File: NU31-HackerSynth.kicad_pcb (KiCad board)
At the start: 2 copper layers, 180 x 110 mm, 135 parts, among them J1 Conn_02x07_Counter_Clockwise, J2 AudioJack3, J3 Barrel_Jack, J4 AudioJack2_SwitchT, J5 AudioJack2_SwitchT, J6 AudioJack2_SwitchT, J7 Eurorack Power, Q1 NPN, Q2 NPN, Q3 NPN, Q4 NPN, SW1 SW_DPDT, SW2 SW_SPDT, U1 LM358, U2 LM358, U3 LM358, U4 CD4017, U5 LM358, U6 LM358, U7 LM358

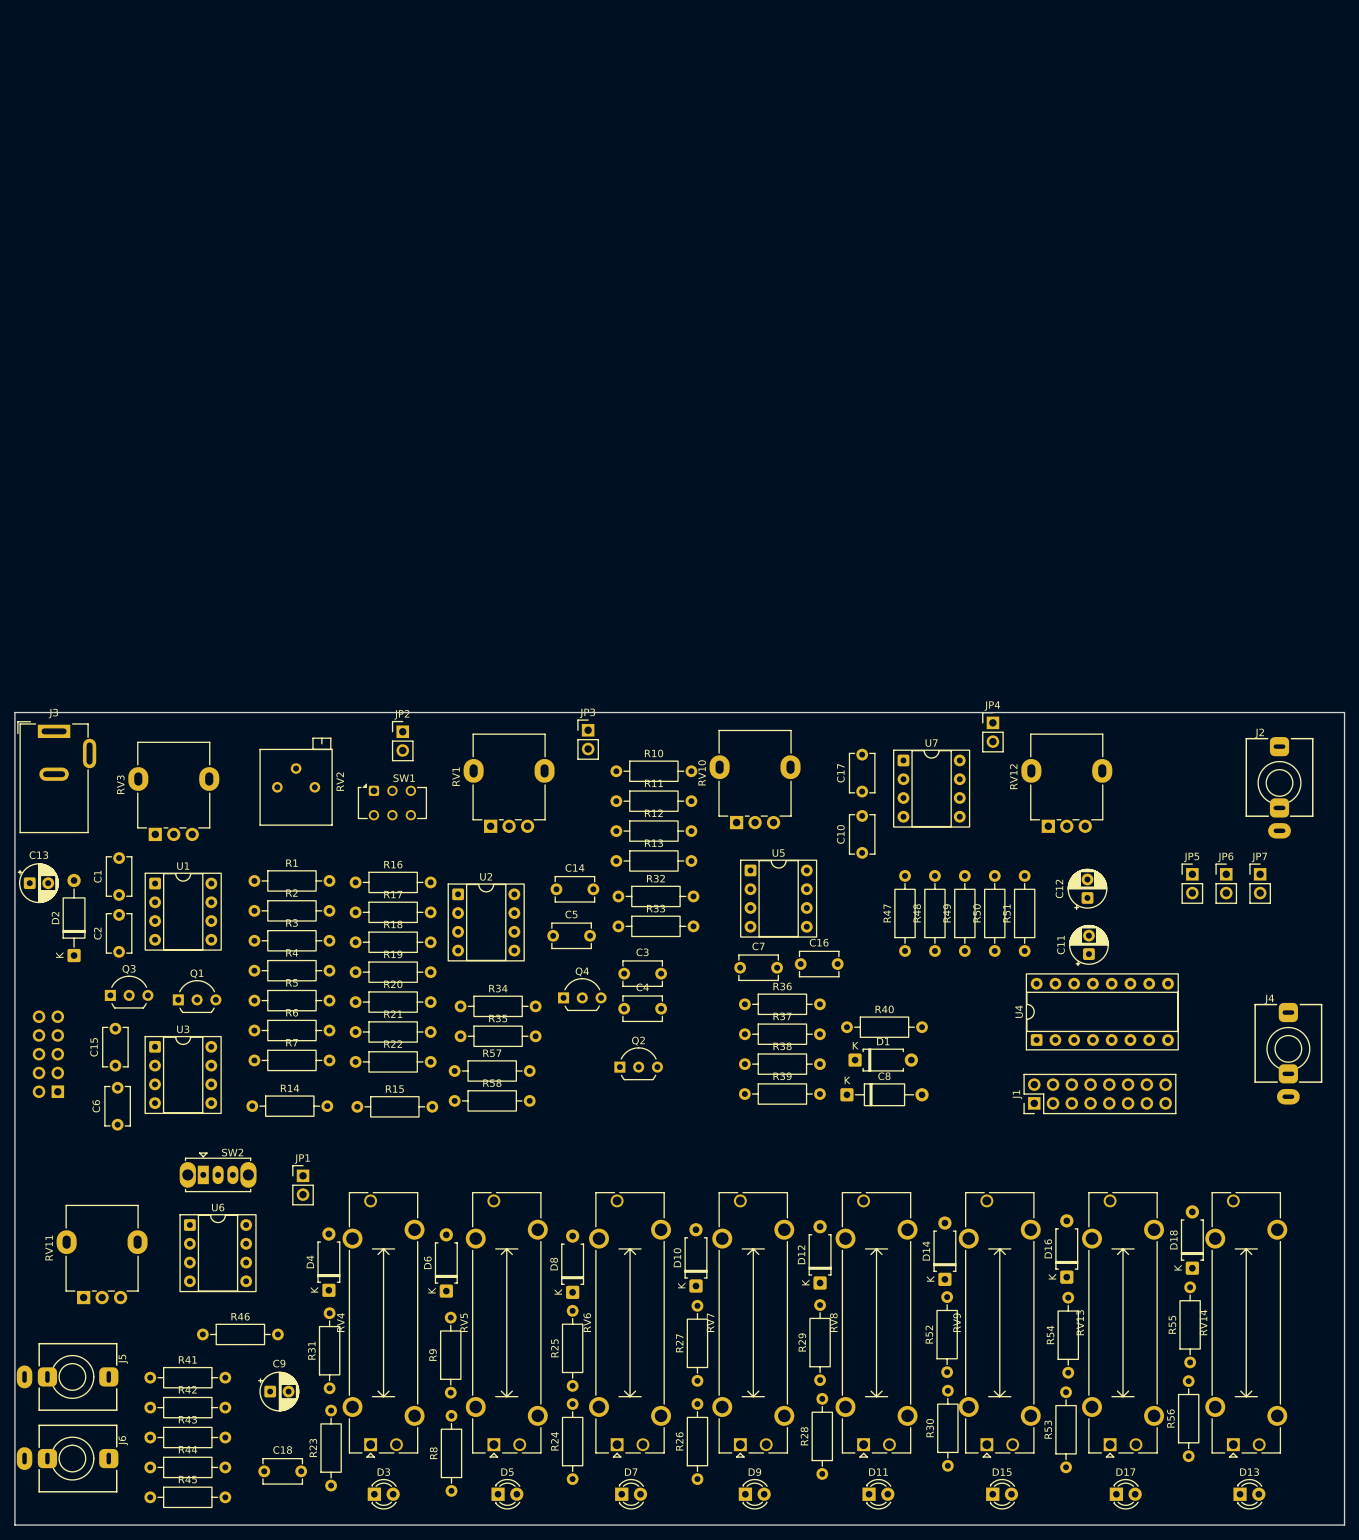
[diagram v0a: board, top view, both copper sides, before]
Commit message: Added negative voltage protection for sequencer clock input, added footprints for faders and rotaryswitch
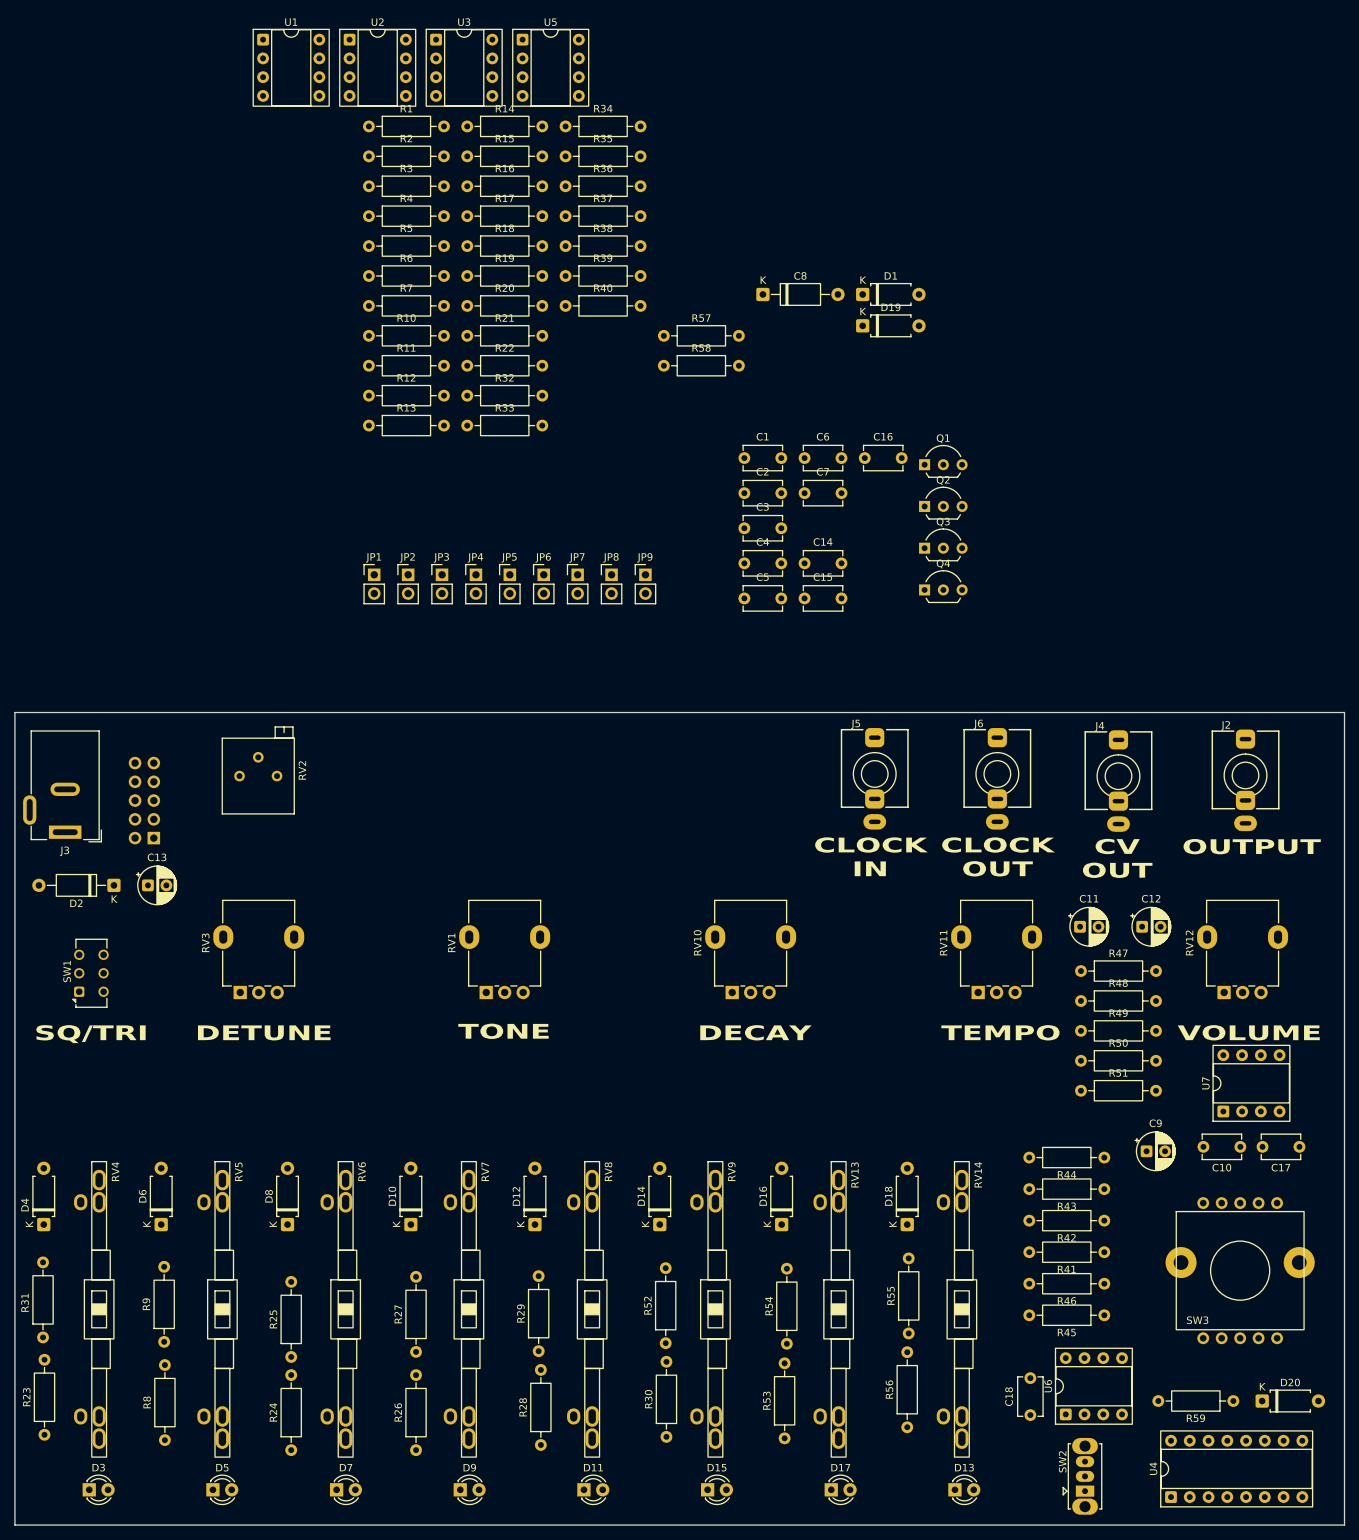
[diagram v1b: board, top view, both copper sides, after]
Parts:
- removed J1: Conn_02x07_Counter_Clockwise, Connector_PinHeader_2.54mm:PinHeader_2x08_P2.54mm_Vertical
- added D19: 1N4148, Diode_THT:D_A-405_P7.62mm_Horizontal, F.Cu at (164.8, -2.35)
- added D20: 1N4148, Diode_THT:D_A-405_P7.62mm_Horizontal, F.Cu at (218.8, 143.2)
- added JP8: Jumper_2_Bridged, Connector_PinHeader_2.54mm:PinHeader_1x02_P2.54mm_Vertical, F.Cu at (130.8, 31.4)
- added JP9: Jumper_2_Bridged, Connector_PinHeader_2.54mm:PinHeader_1x02_P2.54mm_Vertical, F.Cu at (135.4, 31.4)
- added R59: 1k, Resistor_THT:R_Axial_DIN0207_L6.3mm_D2.5mm_P10.16mm_Horizontal, F.Cu at (214.9, 143.2)
- added SW3: SW_Rotary_1x8_MP, SpaceCow:8-way Rotary Switch, F.Cu at (215.9, 125.6)
- C5: value ? -> 10n
- Q1, Q2, Q3, Q4: value NPN -> BC547
- R34, R35: value 10k -> 1k
- RV13, RV14, RV4, RV5, RV6, RV7, RV8, RV9: footprint Potentiometer_THT:Potentiometer_Bourns_PTA2043_Single_Slide -> SpaceCow:40mm Fader Potentiometer (double)
- moved J6 155.8 mm to (183.0, 58.3), turned to 0 degrees
- moved U3 141.6 mm to (107.0, -41.1)
- moved J5 135.9 mm to (166.4, 58.3), turned to 0 degrees
- moved R44 135.8 mm to (197.5, 110.2), turned to 180 degrees
- moved R14 135.8 mm to (111.2, -29.4)
- moved R43 133.5 mm to (197.5, 114.5), turned to 180 degrees
- moved R42 131.6 mm to (197.5, 118.8), turned to 180 degrees
- moved R45 131.5 mm to (197.5, 131.6), turned to 180 degrees
- moved R41 130.3 mm to (197.5, 123.1), turned to 180 degrees
- moved C6 129.6 mm to (156.9, 15.6), turned to 0 degrees
- moved R15 129.5 mm to (111.2, -25.3)
- moved RV11 127.9 mm to (180.4, 87.9)
- moved SW2 126.8 mm to (194.9, 155.4), turned to 90 degrees
- moved Q3 125.8 mm to (173.2, 27.8)
- moved Q1 124.3 mm to (173.2, 16.4)
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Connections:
- R34 pad 2: Net-(R34-Pad2) -> /OSC1_OUT
- R35 pad 2: Net-(R34-Pad2) -> /OSC2_OUT
- RV1 pad 1: Net-(R34-Pad2) -> /MIX_IN
- U4 pad 14: Net-(SW2-B) -> Net-(D20-K)
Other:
- board text added: "CLOCK IN"
- board text added: "CLOCK OUT"
- board text added: "CV OUT"
- board text added: "DECAY"
- board text added: "DETUNE"
- board text added: "OUTPUT"
- board text added: "SQ/TRI"
- board text added: "TEMPO"
- board text added: "TONE"
- board text added: "VOLUME"
- board text removed: "Clock"
- board text removed: "Mixer/Tone"
- board text removed: "Oscillators"
- board text removed: "Output"
- board text removed: "Power"
- board text removed: "VCA/Decay"

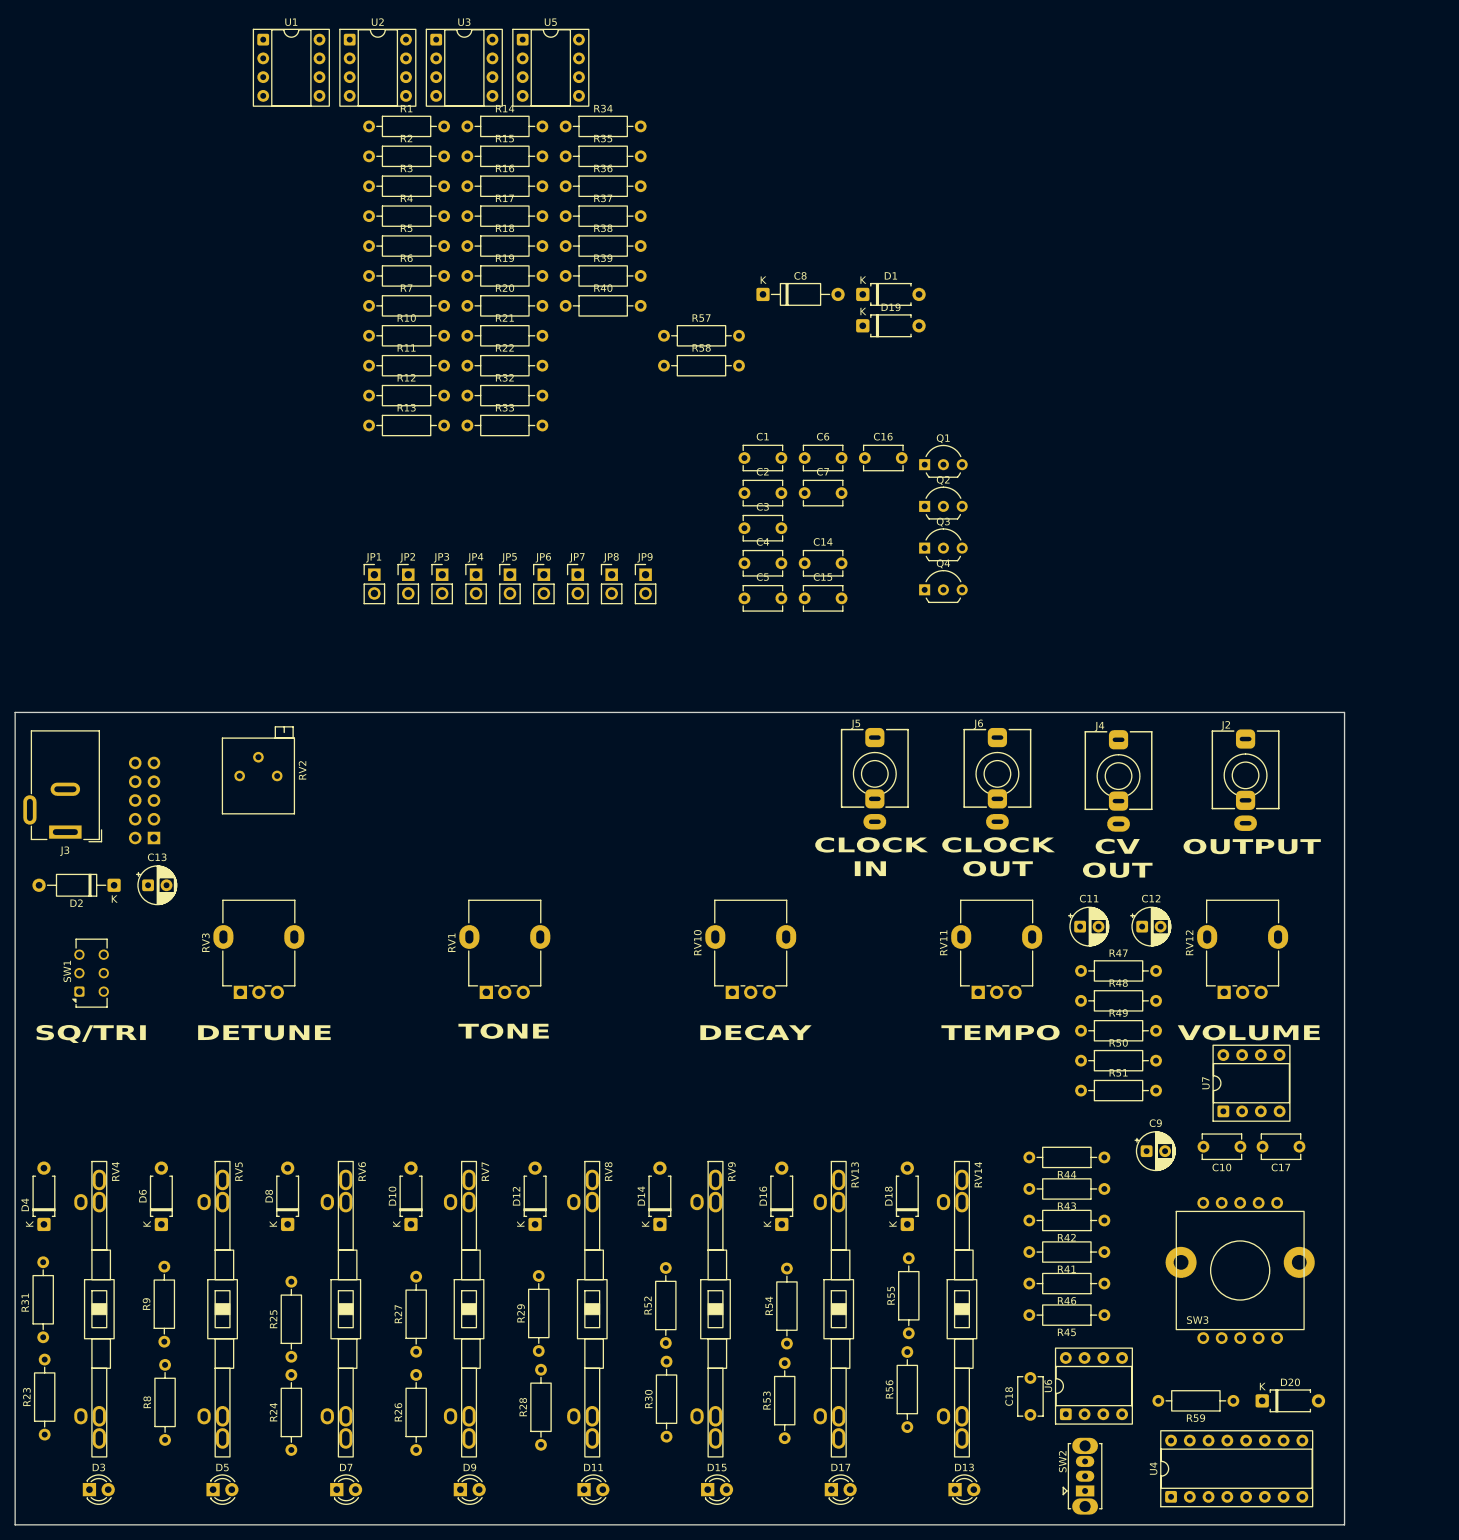
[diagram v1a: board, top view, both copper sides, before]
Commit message: added decoupling cap for CD4017, replaced all routing jumpers with one pin header
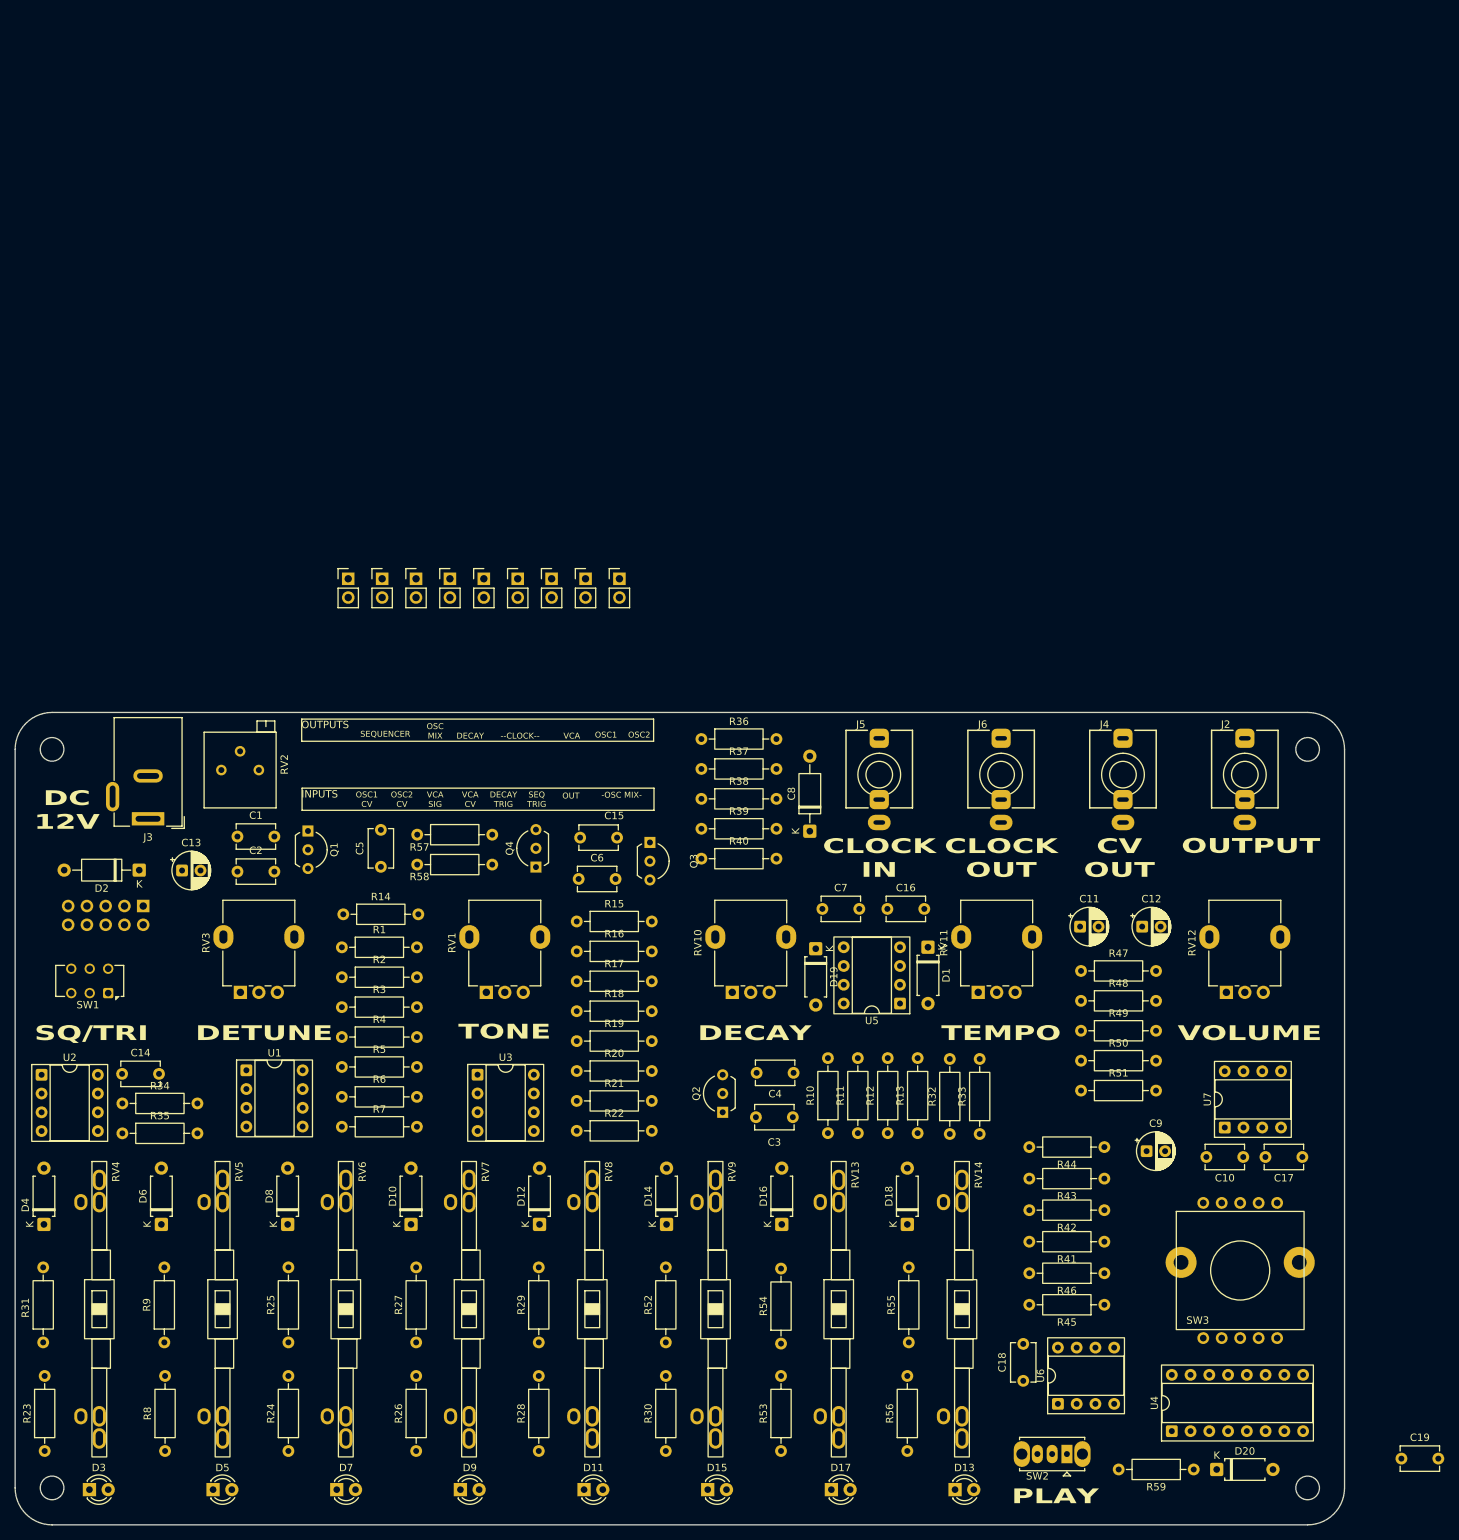
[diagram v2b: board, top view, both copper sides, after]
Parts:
- added C19: 100n, Capacitor_THT:C_Disc_D5.1mm_W3.2mm_P5.00mm, F.Cu at (237.7, 151.0)
- added REF**: MountingHole_3.2mm_M3_DIN965, MountingHole:MountingHole_3.2mm_M3_DIN965, F.Cu at (225.0, 55.0)
- added REF**: MountingHole_3.2mm_M3_DIN965, MountingHole:MountingHole_3.2mm_M3_DIN965, F.Cu at (55.0, 55.0)
- added REF**: MountingHole_3.2mm_M3_DIN965, MountingHole:MountingHole_3.2mm_M3_DIN965, F.Cu at (55.0, 155.0)
- added REF**: MountingHole_3.2mm_M3_DIN965, MountingHole:MountingHole_3.2mm_M3_DIN965, F.Cu at (225.0, 155.0)
- moved U2 146.2 mm to (53.6, 99.1)
- moved R34 145.3 mm to (64.5, 102.9)
- moved R35 145.3 mm to (64.5, 107.0)
- moved U3 140.3 mm to (112.6, 99.0)
- moved U5 140.2 mm to (169.8, 89.4), turned to 180 degrees
- moved U1 139.6 mm to (81.3, 98.5)
- moved R10 124.6 mm to (160.1, 107.0), turned to 90 degrees
- moved R11 123.2 mm to (164.1, 107.0), turned to 90 degrees
- moved R12 122.1 mm to (168.2, 107.0), turned to 90 degrees
- moved R13 121.2 mm to (172.2, 107.0), turned to 90 degrees
- moved R32 119.4 mm to (176.6, 107.1), turned to 90 degrees
- moved R33 118.4 mm to (180.6, 107.1), turned to 90 degrees
- moved C14 115.4 mm to (64.5, 98.9)
- moved R1 111.2 mm to (94.2, 81.8)
- moved R3 111.2 mm to (94.2, 89.9)
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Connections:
- U4 pad 16: VCC -> +VDC
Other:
- outline, holes or cut-outs redrawn
- board text added: "--CLOCK--"
- board text added: "-OSC MIX-"
- board text added: "DC 12V"
- board text added: "DECAY TRIG"
- board text added: "INPUTS"
- board text added: "OSC MIX"
- board text added: "OSC1"
- board text added: "OSC1 CV"
- board text added: "OSC2"
- board text added: "OSC2 CV"
- board text added: "OUT"
- board text added: "OUTPUTS"
- board text added: "PLAY"
- board text added: "SEQ TRIG"
- board text added: "SEQUENCER"
- board text added: "VCA"
- board text added: "VCA CV"
- board text added: "VCA SIG"
